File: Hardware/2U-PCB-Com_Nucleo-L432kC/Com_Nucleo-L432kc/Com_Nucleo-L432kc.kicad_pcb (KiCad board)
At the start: 2 copper layers, 90 x 92 mm, 29 parts, among them IC1 PCI_EXPRESS_CARD, J1 Bus Standard, J2 Calculatrice_UART_groove, J3 RAK5146_UART_groove(GPS), J4 RAK5146_SPI_groove(MCU), J5 RAK5146_I2C_groove(GPS), Q2 BC807

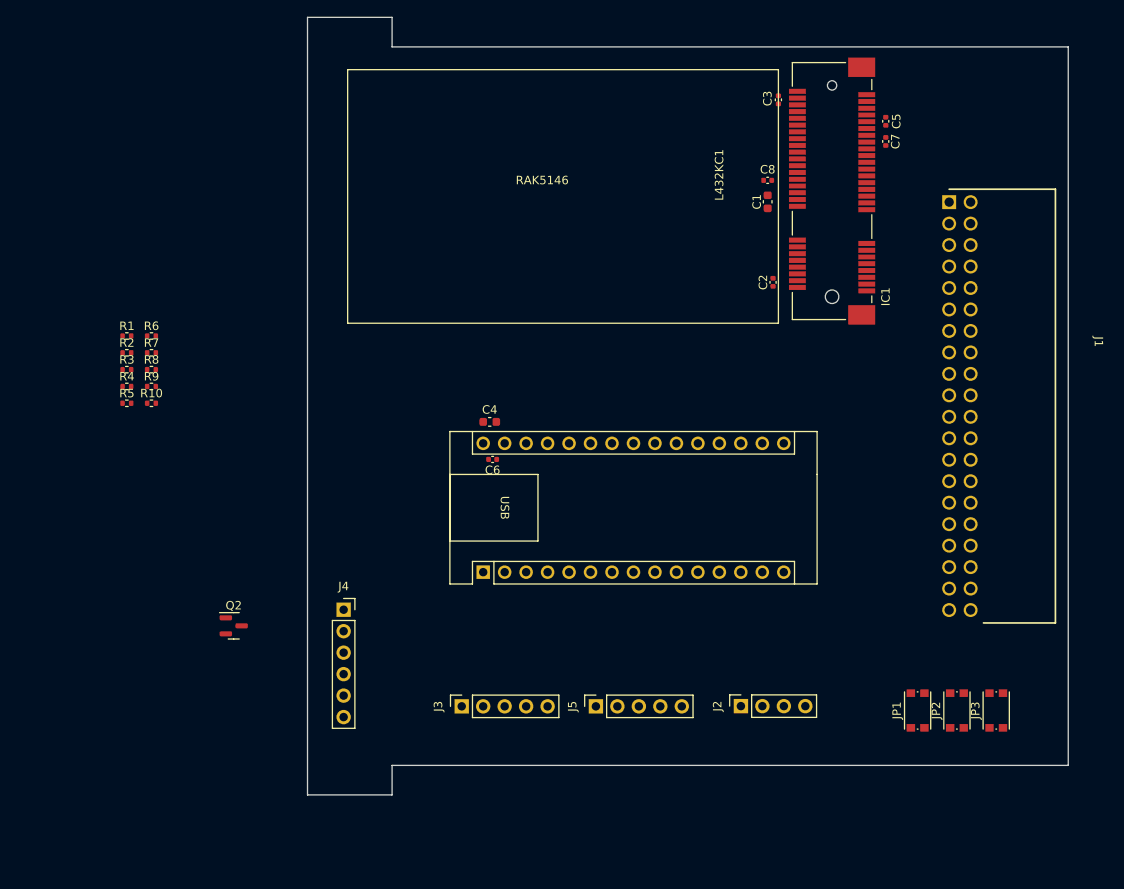
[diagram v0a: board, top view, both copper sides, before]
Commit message: Resistors number fixed. Schematic is ready to start routing. Some power routings are done.
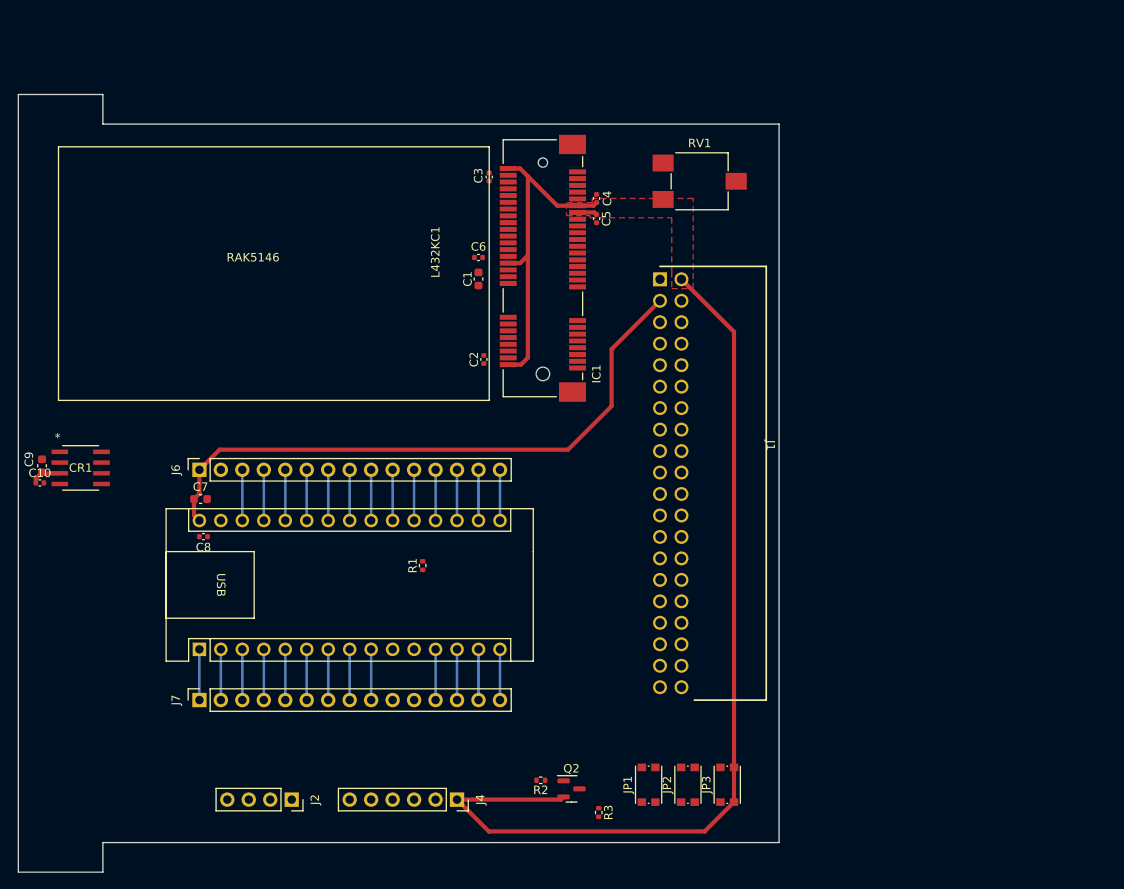
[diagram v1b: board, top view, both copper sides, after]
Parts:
- removed J3: RAK5146_UART_groove(GPS), Connector_PinSocket_2.54mm:PinSocket_1x05_P2.54mm_Vertical
- removed J5: RAK5146_I2C_groove(GPS), Connector_PinSocket_2.54mm:PinSocket_1x05_P2.54mm_Vertical
- removed R10: 100K, Resistor_SMD:R_0402_1005Metric
- removed R4, R5: 0, Resistor_SMD:R_0402_1005Metric
- removed R6, R7, R8: 100, Resistor_SMD:R_0402_1005Metric
- removed R9: 1K, Resistor_SMD:R_0402_1005Metric
- added C10: 100n, Capacitor_SMD:C_0402_1005Metric, F.Cu at (66.3, 89.0)
- added C9: 10u, Capacitor_SMD:C_0603_1608Metric, F.Cu at (66.6, 87.0)
- added CR1: L9616, footprints:SO-8_STM, F.Cu at (71.1, 87.2)
- added J6: Conn_01x15, Connector_PinSocket_2.54mm:PinSocket_1x15_P2.54mm_Vertical, F.Cu at (85.2, 87.5)
- added J7: Conn_01x15, Connector_PinSocket_2.54mm:PinSocket_1x15_P2.54mm_Vertical, F.Cu at (85.2, 114.7)
- added RV1: R_Potentiometer_Trim, Potentiometer_SMD:Potentiometer_ACP_CA6-VSMD_Vertical, F.Cu at (144.4, 53.3)
- JP1: value Jumper_RESET_GPS_Open -> Jumper_RESET_L432KC_Open
- R2: value 100 -> 1K
- R3: value 0 -> 100K
- moved R3 76.6 mm to (132.4, 128.0), turned to -90 degrees
- moved R2 70.4 mm to (125.6, 124.2), turned to 180 degrees
- moved J2 54.3 mm to (96.1, 126.5), turned to -90 degrees
- moved Q2 44.4 mm to (129.2, 125.2)
- moved R1 44.3 mm to (111.6, 98.8), turned to 90 degrees
- moved C1 35.4 mm to (118.2, 64.9)
- moved C4 35.4 mm to (132.2, 55.4)
- moved C5 35.4 mm to (132.2, 57.7)
- moved C6 35.4 mm to (118.2, 62.3)
- moved IC1 35.4 mm to (125.8, 63.6)
- moved J1 35.4 mm to (152.5, 89.0)
- moved C2 35.4 mm to (118.8, 74.4)
- moved C3 35.4 mm to (119.5, 52.8)
- moved C8 35.4 mm to (85.7, 95.4)
- moved C7 35.4 mm to (85.3, 90.9)
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- renumbered C5 to C4, C7 to C5, C8 to C6, C4 to C7, C6 to C8
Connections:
- IC1 pad 19: Net-(IC1-RESERVED) -> unconnected-(IC1-RESERVED-Pad19)
- IC1 pad 22: Net-(IC1-~{PERST}) -> /SX1303_RESET
- IC1 pad 23: Net-(IC1-PERn0) -> unconnected-(IC1-PERn0-Pad23)
- IC1 pad 25: /STANDBY_GPS -> unconnected-(IC1-PERp0-Pad25)
- IC1 pad 28: Net-(IC1-1.5V_2-Pad28) -> /SX1303_GPIO_8
- IC1 pad 30: Net-(IC1-SMB_SCL) -> unconnected-(IC1-SMB_SCL-Pad30)
- IC1 pad 31: /UART_TX_GPS -> unconnected-(IC1-PETn0-Pad31)
- IC1 pad 32: Net-(IC1-SMB_SDA) -> unconnected-(IC1-SMB_SDA-Pad32)
- IC1 pad 33: /UART_RX_GPS -> unconnected-(IC1-PETp0-Pad33)
- IC1 pad 36: /USB_DM -> unconnected-(IC1-USB_D--Pad36)
- IC1 pad 38: /USB_DP -> unconnected-(IC1-USB_D+-Pad38)
- IC1 pad 6: Net-(IC1-1.5V_2-Pad6) -> /GPIO(6)
- JP1 pad 1: /MCU_NRESET -> /L432KC_RESET
- JP3 pad 1: GND -> /SX1303_RESET
- L432KC1 pad 17: unconnected-(L432KC1-+3V3-Pad17) -> Net-(J6-Pin_14)
- L432KC1 pad 18: unconnected-(L432KC1-AREF-Pad18) -> Net-(J6-Pin_13)
- L432KC1 pad 21: /PWM_MAG-Y -> Net-(J6-Pin_10)
- L432KC1 pad 22: unconnected-(L432KC1-A3-Pad22) -> /C_LOW
- L432KC1 pad 26: unconnected-(L432KC1-A7-Pad26) -> /C_HIGH
- L432KC1 pad 27: unconnected-(L432KC1-+5V-Pad27) -> Net-(J6-Pin_4)
- Q2 pad 3: GND -> /SX1303_RESET
- R2 pad 1: /T_PULSE_GPS -> Net-(Q2-B)
- R2 pad 2: Net-(IC1-RESERVED) -> /MCU_NRESET
- R3 pad 1: /MCU_NRESET -> /SX1303_RESET
- R3 pad 2: Net-(IC1-PERn0) -> GND
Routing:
- net +3V3: track 0.00 -> 158.2 mm
- net /Vin: track 0.00 -> 73.2 mm
- net /L432KC_RESET: track 0.00 -> 12.0 mm
- net Net-(J6-Pin_4): track 0.00 -> 6.00 mm
- net Net-(J6-Pin_14): track 0.00 -> 6.00 mm
- net Net-(J6-Pin_13): track 0.00 -> 6.00 mm
- net Net-(J6-Pin_10): track 0.00 -> 6.00 mm
- net GND: track 0.00 -> 6.00 mm
- net /TX_CALC: track 0.00 -> 6.00 mm
- net /SX1303_GPIO_8: track 0.00 -> 6.00 mm
- net /SENS_ROUE/MAG-X: track 0.00 -> 6.00 mm
- net /SENS_MAG-Y: track 0.00 -> 6.00 mm
- net /SDA: track 0.00 -> 6.00 mm
- net /SCL: track 0.00 -> 6.00 mm
- net /RX_CALC: track 0.00 -> 6.00 mm
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- added copper zone on F.Cu, net +3V3

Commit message: Some libraries were added for NAND gate. Also I2C in mikrobus changed. ROuting started respecting constraints.
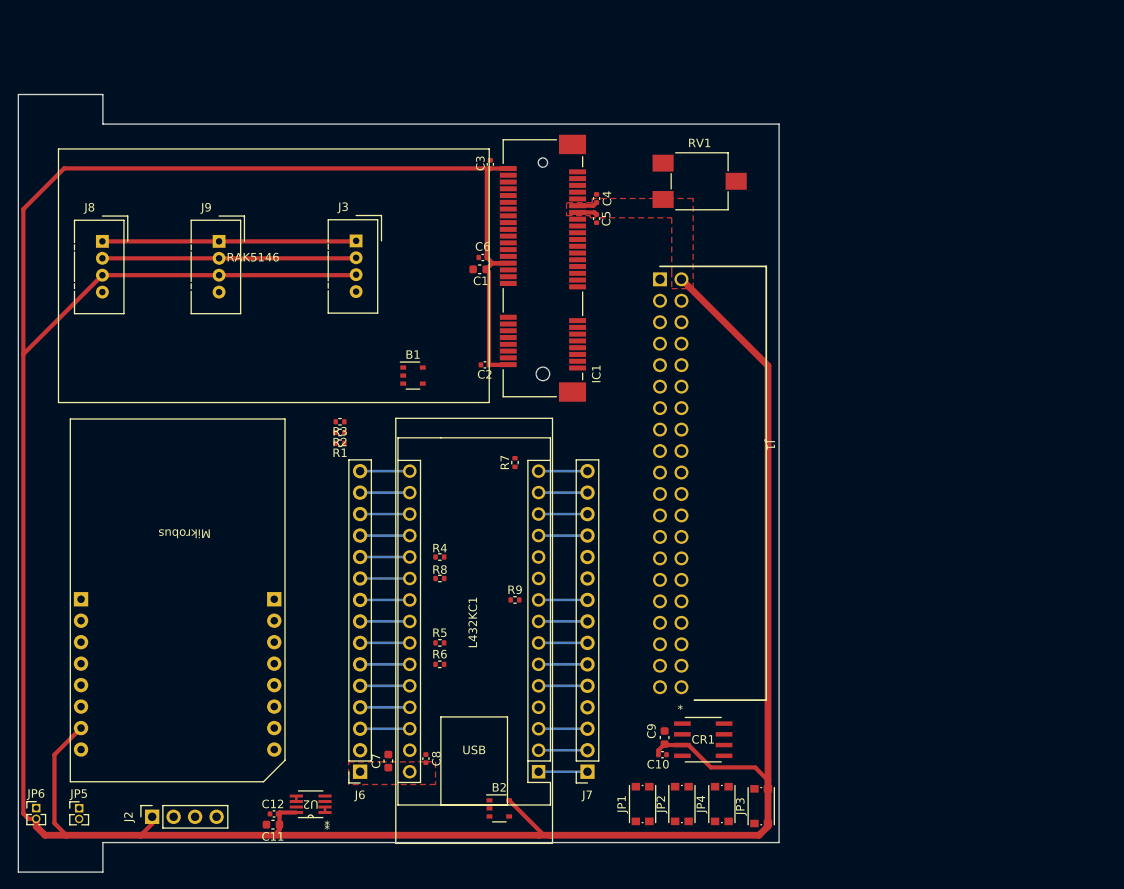
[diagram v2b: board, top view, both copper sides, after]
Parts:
- removed Q2: BC807, Package_TO_SOT_SMD:SOT-23
- added B1: SN74AHC1G125DBVT, Package_SO:TSOP-5_1.65x3.05mm_P0.95mm, F.Cu at (110.4, 76.3)
- added B2: SN74AHC1G125DBVT, Package_SO:TSOP-5_1.65x3.05mm_P0.95mm, F.Cu at (120.7, 127.5)
- added C11: 10u, Capacitor_SMD:C_0603_1608Metric, F.Cu at (93.9, 129.4)
- added C12: 100n, Capacitor_SMD:C_0402_1005Metric, F.Cu at (94.0, 128.2)
- added J3: I2C_Groove, Connector:NS-Tech_Grove_1x04_P2mm_Vertical, F.Cu at (103.7, 60.4)
- added J5: Conn_01x08, Conn_mikro:MIkrobus_Connector, F.Cu at (94.0, 111.7)
- added J8: I2C_Groove, Connector:NS-Tech_Grove_1x04_P2mm_Vertical, F.Cu at (73.7, 60.4)
- added J9: I2C_Groove, Connector:NS-Tech_Grove_1x04_P2mm_Vertical, F.Cu at (87.5, 60.4)
- added JP4: Jumper_RESET_GPS_Open, Button_Switch_SMD:SW_Push_1P1T_NO_CK_KMR2, F.Cu at (147.0, 127.0)
- added JP5: Jumper_STANDBY_GPS_Open, Connector_PinHeader_1.27mm:PinHeader_1x02_P1.27mm_Vertical, F.Cu at (70.9, 127.5)
- added JP6: speed_controller, Connector_PinHeader_1.27mm:PinHeader_1x02_P1.27mm_Vertical, F.Cu at (65.9, 127.5)
- added R4: 100, Resistor_SMD:R_0402_1005Metric, F.Cu at (113.6, 97.8)
- added R5: 100, Resistor_SMD:R_0402_1005Metric, F.Cu at (113.6, 107.9)
- added R6: 100, Resistor_SMD:R_0402_1005Metric, F.Cu at (113.6, 110.5)
- added R7: 100, Resistor_SMD:R_0402_1005Metric, F.Cu at (122.5, 86.6)
- added R8: 0, Resistor_SMD:R_0402_1005Metric, F.Cu at (113.6, 100.3)
- added R9: 0, Resistor_SMD:R_0402_1005Metric, F.Cu at (122.5, 102.8)
- added U2: 74LVC2G02, SN74LVC2G02_SSOP:DCT8, F.Cu at (98.3, 127.0)
- J2: value Calculatrice_UART_groove -> I2C_Groove
- J4: value RAK5146_SPI_groove(MCU) -> Conn_01x08; footprint Connector_PinSocket_2.54mm:PinSocket_1x06_P2.54mm_Vertical -> Conn_mikro:MIkrobus_Connector
- R2: value 1K -> 100
- R3: value 100K -> 0
- moved C10 80.4 mm to (140.0, 121.2)
- moved C9 80.4 mm to (140.2, 119.1)
- moved CR1 80.4 mm to (144.8, 119.4)
- moved R3 55.4 mm to (101.8, 81.8), turned to 180 degrees
- moved R2 47.5 mm to (101.8, 83.0)
- moved J4 46.9 mm to (71.2, 111.7), turned to 0 degrees
- moved J7 46.7 mm to (131.1, 123.2), turned to 180 degrees
- moved L432KC1 42.7 mm to (125.3, 123.2), turned to 180 degrees
- moved J6 40.5 mm to (104.2, 123.2), turned to 180 degrees
- moved C7 38.1 mm to (107.5, 121.9), turned to 90 degrees
- moved C8 37.2 mm to (112.0, 121.6), turned to 90 degrees
- moved R1 17.5 mm to (101.8, 84.3), turned to 180 degrees
- moved J2 16.6 mm to (79.6, 128.5), turned to 90 degrees
- moved JP3 4.76 mm to (151.6, 127.2)
- moved JP1 2.39 mm to (137.6, 127.0)
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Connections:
- CR1 pad 6: /C_LOW -> /CAN_RD
- CR1 pad 7: /C_HIGH -> /CAN_TD
- IC1 pad 19: unconnected-(IC1-RESERVED-Pad19) -> Net-(IC1-RESERVED)
- IC1 pad 23: unconnected-(IC1-PERn0-Pad23) -> Net-(IC1-PERn0)
- IC1 pad 25: unconnected-(IC1-PERp0-Pad25) -> /STANDBY_GPS
- IC1 pad 28: /SX1303_GPIO_8 -> Net-(IC1-1.5V_2-Pad28)
- IC1 pad 30: unconnected-(IC1-SMB_SCL-Pad30) -> /SCL
- IC1 pad 32: unconnected-(IC1-SMB_SDA-Pad32) -> /SDA
- IC1 pad 45: /HOST_SCK -> Net-(IC1-RESERVED1)
- IC1 pad 47: /HOST_MISO -> Net-(IC1-RESERVED2)
- IC1 pad 49: /HOST_MOSI -> Net-(IC1-RESERVED3)
- IC1 pad 51: /HOST_CSN -> Net-(IC1-RESERVED4)
- IC1 pad 6: /GPIO(6) -> Net-(IC1-1.5V_2-Pad6)
- J1 pad 22: unconnected-(J1-RD-Pad22) -> /CAN_RD
- J1 pad 24: unconnected-(J1-TD-Pad24) -> /CAN_TD
- J2 pad 2: /RX_CALC -> /SCL
- J2 pad 3: /TX_CALC -> /SDA
- J4 pad 1: +3V3 -> /AN
- J4 pad 2: /HOST_SCK -> /MCU_NRESET
- J4 pad 3: /HOST_MISO -> /CS_MCU
- J4 pad 4: /HOST_MOSI -> /HOST_SCK
- J4 pad 5: /HOST_CSN -> /MKB_MISO
- J4 pad 6: GND -> /MCU_MOSI
- J6 pad 10: Net-(J6-Pin_10) -> /GPIO(6)
- J6 pad 5: /C_HIGH -> /INT_MKR
- J6 pad 6: /HOST_MOSI -> /MCU_MOSI
- J6 pad 7: /HOST_MISO -> /MISO
- J6 pad 9: /C_LOW -> /AN
- J7 pad 15: /HOST_CSN -> /CS_MCU
- J7 pad 9: /SX1303_GPIO_8 -> /PWM_MKR
- L432KC1 pad 15: /HOST_CSN -> /CS_MCU
- L432KC1 pad 21: Net-(J6-Pin_10) -> /GPIO(6)
- L432KC1 pad 22: /C_LOW -> /AN
- L432KC1 pad 24: /HOST_MISO -> /MISO
- L432KC1 pad 25: /HOST_MOSI -> /MCU_MOSI
- L432KC1 pad 26: /C_HIGH -> /INT_MKR
- L432KC1 pad 9: /SX1303_GPIO_8 -> /PWM_MKR
- R2 pad 1: Net-(Q2-B) -> unconnected-(R2-Pad1)
- R2 pad 2: /MCU_NRESET -> Net-(IC1-RESERVED)
- R3 pad 1: /SX1303_RESET -> /MCU_NRESET
- R3 pad 2: GND -> Net-(IC1-PERn0)
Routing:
- net +3V3: track 158.2 -> 412.7 mm
- net /Vin: track 73.2 -> 0.63 mm
- net /SDA: track 6.00 -> 35.8 mm
- net /SCL: track 6.00 -> 35.8 mm
- net /CS_MCU: track 0.00 -> 6.43 mm
- net Net-(J6-Pin_10): track 6.00 -> 0.00 mm
- net GND: track 6.00 -> 0.00 mm
- net /SX1303_GPIO_8: track 6.00 -> 0.00 mm
- net /HOST_MOSI: track 6.00 -> 0.00 mm
- net /HOST_MISO: track 6.00 -> 0.00 mm
- net /HOST_CSN: track 6.00 -> 0.00 mm
- net /C_LOW: track 6.00 -> 0.00 mm
- net /C_HIGH: track 6.00 -> 0.00 mm
- net /MISO: track 0.00 -> 5.88 mm
- net /MCU_MOSI: track 0.00 -> 5.88 mm
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- added copper zone on F.Cu, net /Vin
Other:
- board text added: "Mikrobus"

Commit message: Traces almost ready, I'm avoiding through holes because it will be done in campus, not with specialized machines. Constraints: 125 um clearence and wire size. It will be not possible completly avoid through holes
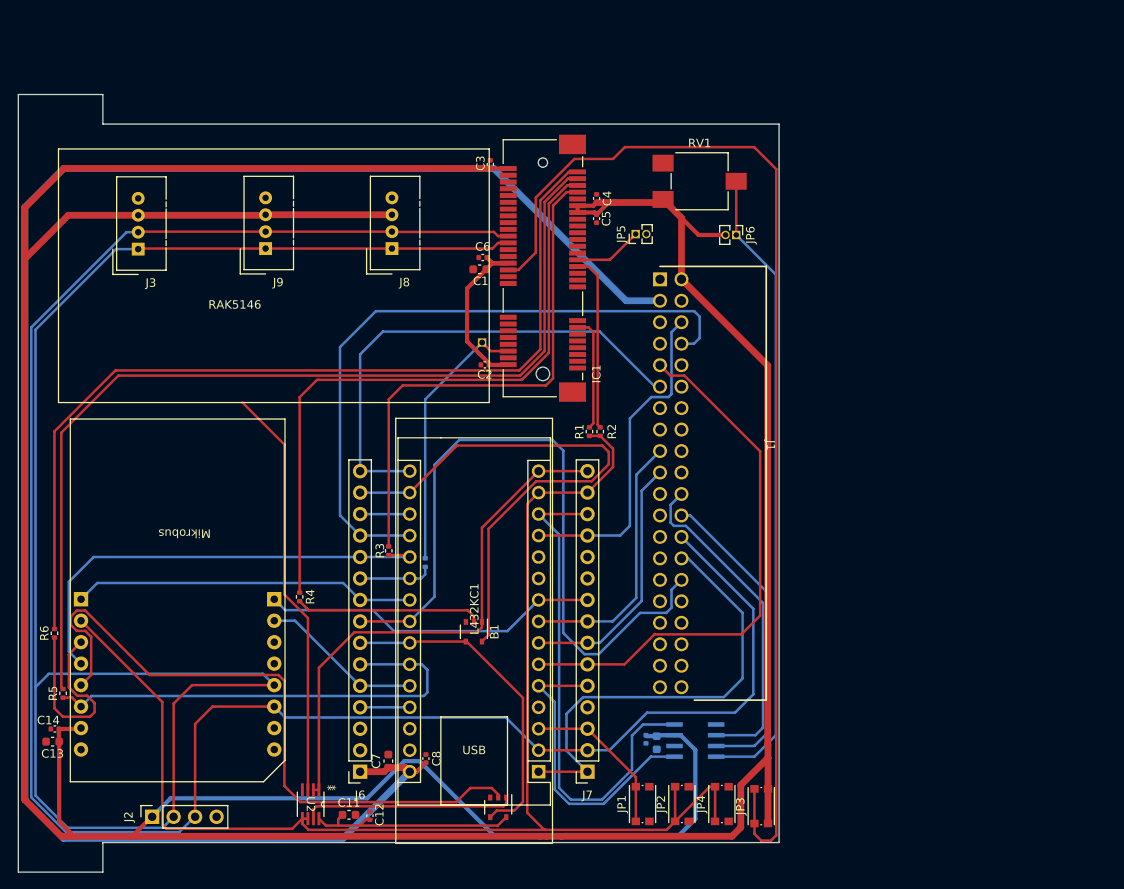
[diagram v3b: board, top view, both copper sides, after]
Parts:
- removed the R2 at (101.8, 83.0)
- removed R9: 0, Resistor_SMD:R_0402_1005Metric
- added C13: 10u, Capacitor_SMD:C_0603_1608Metric, F.Cu at (67.8, 119.6)
- added C14: 100n, Capacitor_SMD:C_0402_1005Metric, F.Cu at (68.1, 118.1)
- added J10: Conn_01x01, Connector_PinSocket_1.27mm:PinSocket_1x01_P1.27mm_Vertical, F.Cu at (118.6, 72.4)
- C10, C9, CR1: moved to B.Cu
- J2, J3, J8, J9: value I2C_Groove -> I2C_Grove
- R7: renamed from R8; moved to B.Cu
- moved JP6 107.0 mm to (148.7, 59.7), turned to -90 degrees
- moved JP5 94.6 mm to (136.8, 59.6), turned to 90 degrees
- moved R6 58.1 mm to (68.0, 106.8)
- moved R5 44.7 mm to (69.0, 113.9), turned to 90 degrees
- moved J8 34.3 mm to (108.0, 61.3), turned to 180 degrees
- moved B1 31.1 mm to (117.6, 106.6), turned to -90 degrees
- moved R2 30.8 mm to (132.6, 82.9), turned to 90 degrees
- moved R1 29.5 mm to (131.3, 82.9), turned to 90 degrees
- moved J3 25.8 mm to (77.9, 61.3), turned to 180 degrees
- moved R4 17.5 mm to (97.0, 102.5), turned to 90 degrees
- moved C12 11.3 mm to (105.3, 128.4), turned to 90 degrees
- moved C11 9.07 mm to (102.9, 128.3), turned to 0 degrees
- moved R3 6.09 mm to (107.6, 97.0), turned to 90 degrees
- moved J9 5.57 mm to (93.0, 61.3), turned to 180 degrees
- moved C10 2.67 mm to (138.0, 119.3), turned to -90 degrees
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- renumbered R3 to R2, R4 to R3, R5 to R4, R6 to R5, R7 to R6
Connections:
- net Net-(IC1-1.5V_2-Pad6) renamed /TH1
- net Net-(J6-Pin_13) renamed /AREF
- IC1 pad 19: Net-(IC1-RESERVED) -> unconnected-(IC1-RESERVED-Pad19)
- IC1 pad 28: Net-(IC1-1.5V_2-Pad28) -> unconnected-(IC1-1.5V_2-Pad28)
- J6 pad 14: Net-(J6-Pin_14) -> +3V3
- J6 pad 3: /L432KC_RESET -> unconnected-(J6-Pin_3-Pad3)
- L432KC1 pad 17: Net-(J6-Pin_14) -> +3V3
- L432KC1 pad 28: /L432KC_RESET -> unconnected-(L432KC1-RESET-Pad28)
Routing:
- net /Vin: track 0.63 -> 213.6 mm
- net /SDA: track 35.8 -> 243.7 mm
- net /SCL: track 35.8 -> 243.3 mm
- net /SX1303_RESET: track 0.00 -> 179.0 mm
- net +3V3: track 412.7 -> 590.7 mm
- net /MCU_NRESET: track 6.43 -> 163.1 mm
- net Net-(IC1-RESERVED3): track 0.00 -> 114.3 mm
- net Net-(IC1-RESERVED4): track 0.00 -> 108.3 mm
- net /CS_MCU: track 6.43 -> 88.0 mm
- net /MKB_MISO: track 0.00 -> 79.1 mm
- net /RESET_SIGNAL: track 5.88 -> 84.1 mm
- net Net-(IC1-RESERVED2): track 0.00 -> 76.7 mm
- net Net-(CR1-ASC): track 0.00 -> 75.6 mm
- net /SENS_ROUE/MAG-X: track 5.88 -> 78.7 mm
- net Net-(IC1-RESERVED1): track 0.00 -> 61.9 mm
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- removed copper zone on F.Cu, net +3V3
- removed copper zone on F.Cu, net /Vin
